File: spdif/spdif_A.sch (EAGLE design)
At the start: 23 parts, among them U1 NC7WZ240, U2 NC7WZ240, U3 FIN1002, U4 NC7SZ175, U5 NC7SZ175

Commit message: spdif: WIP schematic
Signed-off-by: malo <pavol.malosek@gmail.com>
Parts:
- added C10, C11, C12, C13, C9: 100n, 0603, rcl:C-EUC0603
- added D1: PESD0603-240, 25cmsquare:ZDPESD0603-240
- added FB1, FB2: (no value), 25cmsquare:FB_0603
- added JP1, JP2: (no value), 25pinhead:PINHD-2X6/90
- added PWR: (no value), 25cmsquare:LIWE_12_PIN_PWR7X7_COMPAT
- added R11, R20: 22R, 0603, rcl:R-EU_R0603
- added R12, R13, R18: 220R, 0603, rcl:R-EU_R0603
- added R14, R15: 1k5, 0603, rcl:R-EU_R0603
- added R16: 100R, 0603, rcl:R-EU_R0603
- added R17, R19: 75R, 0603, rcl:R-EU_R0603
- added RX0: PLR135/T10, 25cmsquare:PLR135_T10
- added RX1, RX2, TX1, TX2: RCJ-01X, CP-1400-ND, 25cmsquare:RCJ-01X
- added T1, T2: DA101MC, 25cmsquare:DA101MC
- added TP0, TP1, TP10, TP11, TP12, TP13, TP2, TP3, TP4, TP5, TP6, TP7, TP8, TP9: TPB1,27, testpad:TPB1,27
- added TX0: PLT133/T10W, 25cmsquare:PLT133_T10W
- added U6: FIN1002, 25cmsquare:FIN1002
- R3: value 22R, 0603 -> 75R, 0603
- U1: value NC7WZ240 -> NC7SZ175; device 25cmsquare:NC7WZ240 -> 25cmsquare:NC7SZ175
- U2: value NC7WZ240 -> FIN1001; device 25cmsquare:NC7WZ240 -> 25cmsquare:FIN1001
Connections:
- removed net CLK: U4.CP, U5.CP
- removed net NSEL_0: U1_A.~OE1
- removed net NSEL_1: U1_B.~OE1
- removed net NSEL_2: U2_A.~OE1
- removed net NSEL_3: U2_B.~OE1
- removed net SPDIF_IN: R3.2
- removed net TX_COAXIAL: U5.D
- removed net TX_OPTICAL: U4.D
- new net +1V0: PWR.2
- new net +2V5: PWR.1
- new net +5V: PWR.6
- new net CLK_0: JP2.3, U4.CP
- new net CLK_1: JP2.7, U5.CP
- new net CLK_2: JP2.11, U1.CP
- new net N$13: C7.1, R13.2
- new net N$16: R15.2, R16.2, T1.4, TP2.TP, U6.RIN-
- new net N$17: R14.1, R16.1, T1.6, TP3.TP, U6.RIN+
- new net N$18: R12.1, R19.2, T2.1
- new net N$19: R3.1, T2.6, TX2.SIG
- new net N$20: R17.2, RX1.GND1, RX1.GND2, RX1.GND3, T1.3
- new net N$21: R17.1, RX1.SIG, T1.1
- new net N$22: R3.2, T2.4, TX2.GND1, TX2.GND2, TX2.GND3
- new net N$23: R18.2, TP12.TP, U2.ROUT-
- new net N$24: R20.1, TP10.TP, U2.RIN
- new net SPDIF0_IN: R1.1, RX0.OUT
- new net SPDIF_IN_0: JP1.1, JP1.3, R1.2, TP1.TP
- new net SPDIF_IN_1: JP1.5, JP1.7, R11.2, TP4.TP
- new net SPDIF_IN_2: JP1.11, JP1.9, R2.2, TP8.TP
- new net SPDIF_OUT_0: JP2.1, U4.D
- new net SPDIF_OUT_1: JP2.5, U5.D
- new net SPDIF_OUT_2: JP2.9, U1.D
- net +3V3: now also C1.2, C10.2, C12.2, C13.2, C2.2, FB1.P$2, FB2.P$2, PWR.4, R14.2, U1.VCC, U1.~C, U2.VCC, U6.VCC; no longer C1.1, C2.1, U1_PWR.VCC, U2_PWR.VCC
- net GND: now also C1.1, C10.1, C11.1, C12.1, C13.1, C2.1, C9.1, D1.A, JP1.10, JP1.12, JP1.2, JP1.4, JP1.6, JP1.8, JP2.10, JP2.12, JP2.2, JP2.4, JP2.6, JP2.8, PWR.3, PWR.8, R15.1, RX0.GND, RX2.GND1, RX2.GND2, RX2.GND3, TX0.GND, TX1.GND1, TX1.GND2, TX1.GND3, U1.GND, U2.GND, U6.GND; no longer C1.2, C2.2, U1_PWR.GND, U2_PWR.GND
- net N$1: now also R20.2, U1.Q; no longer R1.2, U1_A.A1
- net N$10: now also R12.2, TP11.TP, U2.ROUT+; no longer R2.2, U2_B.A1
- net N$11: now also TP7.TP
- net N$12: now also TP6.TP
- net N$14: now also TP9.TP, TX0.IN
- net N$2: now also R18.1, R19.1, T2.3; no longer U1_B.A1
- net N$4: now also TP5.TP
- net N$5: now also C9.2, FB1.P$1, RX0.VCC; no longer R3.1, U1_A.Y1, U1_B.Y1, U2_A.Y1, U2_B.Y1
- net N$6: now also D1.C, RX2.SIG
- net N$7: now also R11.1, U6.ROUT; no longer R1.1
- net N$8: now also R13.1, TP13.TP, TX1.SIG; no longer C7.1
- net N$9: now also C11.2, FB2.P$1, TX0.VCC; no longer U2_A.A1
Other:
- note added: "16.11.22.A"
- moved on the sheet: C3, C4, C5, C6, C7, C8, R1, R10, R2, R4, R5, R6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

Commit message: spdif: WIP pcb
Signed-off-by: malo <pavol.malosek@gmail.com>
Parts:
- removed TP0: TPB1,27, testpad:TPB1,27
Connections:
- net N$1 renamed Q
- net N$10 renamed FIN_OUT_P
- net N$14 renamed TX0_IN
- net N$18 renamed DA_P
- net N$19 renamed TX2_P
- net N$2 renamed DA_N
- net N$22 renamed TX2_N
- net N$23 renamed FIN_OUT_N
- net N$24 renamed FIN_IN
- net N$9 renamed TX0_VCC
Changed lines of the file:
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@@
 <grid distance="0.1" unitdist="inch" unit="inch" style="lines" multiple="1" display="no" altdistance="0.01" altunitdist="inch" altunit="inch"/>
 <layers>
-<layer number="1" name="Top" color="4" fill="1" visible="yes" active="no"/>
-<layer number="16" name="Bottom" color="1" fill="1" visible="yes" active="no"/>
-<layer number="17" name="Pads" color="2" fill="1" visible="yes" active="no"/>
-<layer number="18" name="Vias" color="2" fill="1" visible="yes" active="no"/>
-<layer number="19" name="Unrouted" color="6" fill="1" visible="yes" active="no"/>
-<layer number="20" name="Dimension" color="15" fill="1" visible="yes" active="no"/>
-<layer number="21" name="tPlace" color="7" fill="1" visible="yes" active="no"/>
-<layer number="22" name="bPlace" color="7" fill="1" visible="yes" active="no"/>
-<layer number="23" name="tOrigins" color="15" fill="1" visible="yes" active="no"/>
-<layer number="24" name="bOrigins" color="15" fill="1" visible="yes" active="no"/>
-<layer number="25" name="tNames" color="7" fill="1" visible="yes" active="no"/>
-<layer number="26" name="bNames" color="7" fill="1" visible="yes" active="no"/>
-<layer number="27" name="tValues" color="7" fill="1" visible="yes" active="no"/>
-<layer number="28" name="bValues" color="7" fill="1" visible="yes" active="no"/>
+<layer number="1" name="Top" color="4" fill="1" visible="no" active="no"/>
+<layer number="16" name="Bottom" color="1" fill="1" visible="no" active="no"/>
+<layer number="17" name="Pads" color="2" fill="1" visible="no" active="no"/>
+<layer number="18" name="Vias" color="2" fill="1" visible="no" active="no"/>
+<layer number="19" name="Unrouted" color="6" fill="1" visible="no" active="no"/>
+<layer number="20" name="Dimension" color="15" fill="1" visible="no" active="no"/>
+<layer number="21" name="tPlace" color="7" fill="1" visible="no" active="no"/>
+<layer number="22" name="bPlace" color="7" fill="1" visible="no" active="no"/>
+<layer number="23" name="tOrigins" color="15" fill="1" visible="no" active="no"/>
+<layer number="24" name="bOrigins" color="15" fill="1" visible="no" active="no"/>
+<layer number="25" name="tNames" color="7" fill="1" visible="no" active="no"/>
+<layer number="26" name="bNames" color="7" fill="1" visible="no" active="no"/>
+<layer number="27" name="tValues" color="7" fill="1" visible="no" active="no"/>
+<layer number="28" name="bValues" color="7" fill="1" visible="no" active="no"/>
 <layer number="29" name="tStop" color="7" fill="3" visible="no" active="no"/>
 <layer number="30" name="bStop" color="7" fill="6" visible="no" active="no"/>
@@
 <layer number="35" name="tGlue" color="7" fill="4" visible="no" active="no"/>
 <layer number="36" name="bGlue" color="7" fill="5" visible="no" active="no"/>
-<layer number="37" name="tTest" color="7" fill="1" visible="yes" active="no"/>
-<layer number="38" name="bTest" color="7" fill="1" visible="yes" active="no"/>
+<layer number="37" name="tTest" color="7" fill="1" visible="no" active="no"/>
+<layer number="38" name="bTest" color="7" fill="1" visible="no" active="no"/>
 <layer number="39" name="tKeepout" color="4" fill="11" visible="no" active="no"/>
 <layer number="40" name="bKeepout" color="1" fill="11" visible="no" active="no"/>
@@
 <layer number="44" name="Drills" color="7" fill="1" visible="no" active="no"/>
 <layer number="45" name="Holes" color="7" fill="1" visible="no" active="no"/>
-<layer number="46" name="Milling" color="3" fill="1" visible="yes" active="no"/>
-<layer number="47" name="Measures" color="7" fill="1" visible="yes" active="no"/>
-<layer number="48" name="Document" color="7" fill="1" visible="yes" active="no"/>
-<layer number="49" name="Reference" color="7" fill="1" visible="yes" active="no"/>
-<layer number="50" name="dxf" color="7" fill="1" visible="yes" active="no"/>
-<layer number="51" name="tDocu" color="7" fill="1" visible="yes" active="no"/>
-<layer number="52" name="bDocu" color="7" fill="1" visible="yes" active="no"/>
-<layer number="53" name="tGND_GNDA" color="7" fill="9" visible="yes" active="no"/>
-<layer number="54" name="bGND_GNDA" color="1" fill="9" visible="yes" active="no"/>
-<layer number="56" name="wert" color="7" fill="1" visible="yes" active="no"/>
-<layer number="57" name="tCAD" color="7" fill="1" visible="yes" active="no"/>
-<layer number="59" name="Invisible" color="7" fill="1" visible="yes" active="no"/>
-<layer number="61" name="stand" color="7" fill="1" visible="yes" active="no"/>
+<layer number="46" name="Milling" color="3" fill="1" visible="no" active="no"/>
+<layer number="47" name="Measures" color="7" fill="1" visible="no" active="no"/>
+<layer number="48" name="Document" color="7" fill="1" visible="no" active="no"/>
+<layer number="49" name="Reference" color="7" fill="1" visible="no" active="no"/>
+<layer number="50" name="dxf" color="7" fill="1" visible="no" active="no"/>
+<layer number="51" name="tDocu" color="7" fill="1" visible="no" active="no"/>
+<layer number="52" name="bDocu" color="7" fill="1" visible="no" active="no"/>
+<layer number="53" name="tGND_GNDA" color="7" fill="9" visible="no" active="no"/>
+<layer number="54" name="bGND_GNDA" color="1" fill="9" visible="no" active="no"/>
+<layer number="56" name="wert" color="7" fill="1" visible="no" active="no"/>
+<layer number="57" name="tCAD" color="7" fill="1" visible="no" active="no"/>
+<layer number="59" name="Invisible" color="7" fill="1" visible="no" active="no"/>
+<layer number="61" name="stand" color="7" fill="1" visible="no" active="no"/>
 <layer number="90" name="Modules" color="5" fill="1" visible="yes" active="yes"/>
 <layer number="91" name="Nets" color="2" fill="1" visible="yes" active="yes"/>
@@
 <part name="T1" library="25cmsquare" deviceset="DA" device="101MC"/>
 <part name="T2" library="25cmsquare" deviceset="DA" device="101MC"/>
-<part name="TP0" library="testpad" deviceset="TP" device="B1,27"/>
 <part name="TP1" library="testpad" deviceset="TP" device="B1,27"/>
 <part name="TP2" library="testpad" deviceset="TP" device="B1,27"/>
@@
 <instance part="GND26" gate="1" x="144.78" y="129.54"/>
 <instance part="T1" gate="G$1" x="152.4" y="96.52"/>
-<instance part="TP0" gate="G$1" x="104.14" y="121.92"/>
 <instance part="TP1" gate="G$1" x="83.82" y="96.52" rot="R180"/>
 <instance part="TP2" gate="G$1" x="180.34" y="91.44" rot="R180"/>
@@
 </segment>
 </net>
-<net name="N$14" class="0">
+<net name="TX0_IN" class="0">
 <segment>
 <pinref part="U4" gate="&gt;NAME" pin="Q"/>
@@
 </segment>
 </net>
-<net name="N$9" class="0">
+<net name="TX0_VCC" class="0">
 <segment>
 <pinref part="C11" gate="G$1" pin="2"/>
@@
 </segment>
 </net>
-<net name="N$19" class="0">
+<net name="TX2_P" class="0">
 <segment>
 <pinref part="TX2" gate="G$1" pin="SIG"/>
@@
 </segment>
 </net>
-<net name="N$22" class="0">
+<net name="TX2_N" class="0">
 <segment>
 <pinref part="TX2" gate="G$1" pin="GND1"/>
@@
 </segment>
 </net>
-<net name="N$2" class="0">
+<net name="DA_N" class="0">
 <segment>
 <wire x1="124.46" y1="137.16" x2="121.92" y2="137.16" width="0.1524" layer="91"/>
@@
 </segment>
 </net>
-<net name="N$10" class="0">
+<net name="FIN_OUT_P" class="0">
 <segment>
 <pinref part="U2" gate="G$1" pin="ROUT+"/>
@@
 </segment>
 </net>
-<net name="N$18" class="0">
+<net name="DA_P" class="0">
 <segment>
 <pinref part="R12" gate="G$1" pin="1"/>
@@
 </segment>
 </net>
-<net name="N$23" class="0">
+<net name="FIN_OUT_N" class="0">
 <segment>
 <pinref part="R18" gate="G$1" pin="2"/>
@@
 </segment>
 </net>
-<net name="N$1" class="0">
+<net name="Q" class="0">
 <segment>
 <pinref part="U1" gate="&gt;NAME" pin="Q"/>
@@
 </segment>
 </net>
-<net name="N$24" class="0">
+<net name="FIN_IN" class="0">
 <segment>
 <pinref part="R20" gate="G$1" pin="1"/>

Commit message: spdif: finished PCB
Signed-off-by: malo <pavol.malosek@gmail.com>
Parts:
- removed R16: 100R, 0603, rcl:R-EU_R0603
- removed R19, R3: 75R, 0603, rcl:R-EU_R0603
- added 3V3, GND, GND33: TEST-22-MULTICOMP, 25cmsquare:TEST-22-MULTICOMP
- R12, R18: value 220R, 0603 -> 36R, 0603
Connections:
- net +3V3: now also 3V3.1
- net DA_N: no longer R19.1
- net DA_P: no longer R19.2
- net GND: now also GND.1, GND33.1, RX1.GND1, RX1.GND2, RX1.GND3; no longer RX2.GND1, RX2.GND2, RX2.GND3
- net N$16: no longer R16.2
- net N$17: no longer R16.1
- net N$20: now also RX2.GND2; no longer RX1.GND1, RX1.GND2, RX1.GND3
- net N$21: now also RX2.SIG; no longer RX1.SIG
- net N$6: now also RX1.SIG; no longer RX2.SIG
- net SPDIF_IN_0: now also JP1.11, JP1.9; no longer JP1.1, JP1.3
- net SPDIF_IN_1: now also R2.2, TP8.TP; no longer R11.2, TP4.TP
- net SPDIF_IN_2: now also JP1.1, JP1.3, R11.2, TP4.TP; no longer JP1.11, JP1.9, R2.2, TP8.TP
- net TX2_N: no longer R3.2, TX2.GND2, TX2.GND3
- net TX2_P: no longer R3.1
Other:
- moved on the sheet: R12, R14, R15, R17, R18, RX1, RX2, T1, T2, TP11, TP12, TX2

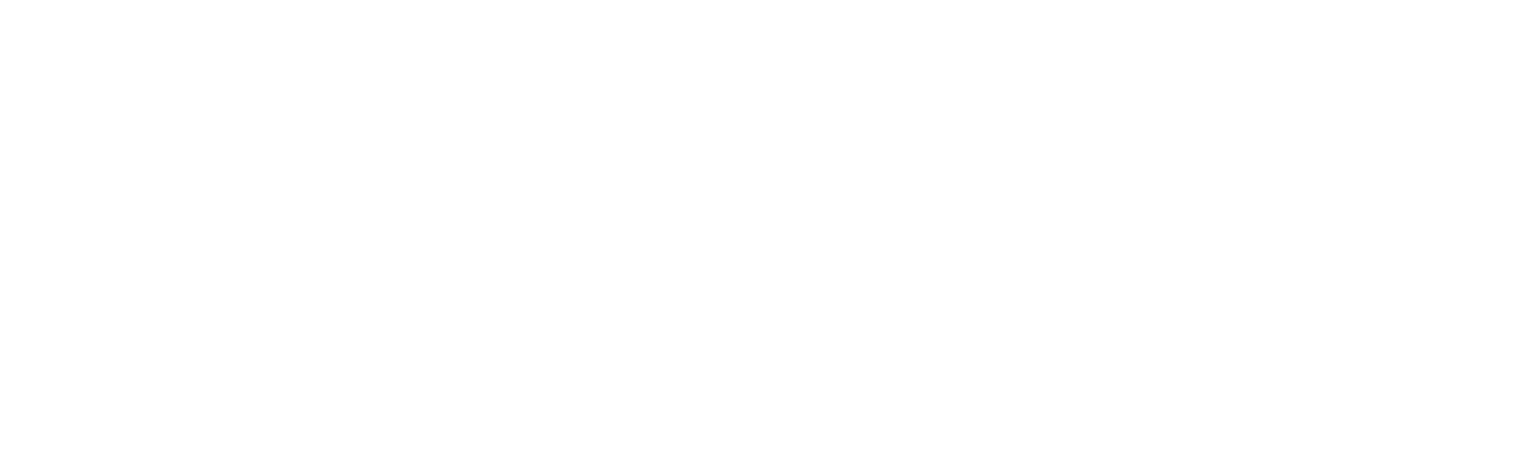
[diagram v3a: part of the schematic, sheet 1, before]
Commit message: spdif: added partlist for digikey
Signed-off-by: malo <pavol.malosek@gmail.com>
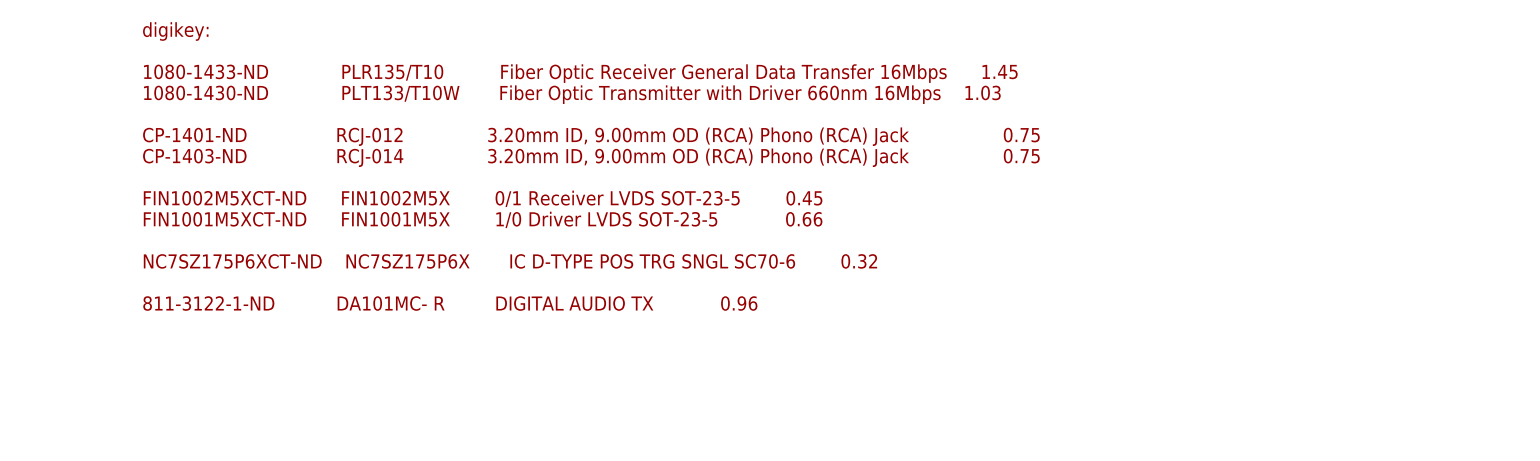
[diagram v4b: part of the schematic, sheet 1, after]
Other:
- note added: "digikey: 1080-1433-ND PLR135/T10 Fiber Optic Receiver General Data Transfer 16Mbps 1.45 1080-1430-ND PLT133/T10W Fiber Optic Transmitter with Driver 660nm 16Mbps 1.03 CP-1401-ND RCJ-012 3.20mm ID, 9.00mm OD (RCA) Phono (RCA) Jack 0.75 CP-1403-ND RCJ-014 3.20mm ID, 9.00mm OD (RCA) Phono (RCA) Jack 0.75 FIN1002M5XCT-ND FIN1002M5X 0/1 Receiver LVDS SOT-23-5 0.45 FIN1001M5XCT-ND FIN1001M5X 1/0 Driver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"
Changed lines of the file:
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@@
 <plain>
 <text x="167.64" y="10.16" size="6.4516" layer="94">16.11.22.A</text>
+<text x="266.7" y="134.62" size="1.778" layer="94">digikey:
+1080-1433-ND             PLR135/T10          Fiber Optic Receiver General Data Transfer 16Mbps  	1.45
+1080-1430-ND             PLT133/T10W       Fiber Optic Transmitter with Driver 660nm 16Mbps	1.03
+CP-1401-ND                RCJ-012               3.20mm ID, 9.00mm OD (RCA) Phono (RCA) Jack                 0.75
+CP-1403-ND                RCJ-014               3.20mm ID, 9.00mm OD (RCA) Phono (RCA) Jack                 0.75
+FIN1002M5XCT-ND      FIN1002M5X        0/1 Receiver LVDS SOT-23-5		0.45
+FIN1001M5XCT-ND      FIN1001M5X        1/0 Driver LVDS SOT-23-5			0.66
+NC7SZ175P6XCT-ND    NC7SZ175P6X       IC D-TYPE POS TRG SNGL SC70-6		0.32
+811-3122-1-ND           DA101MC- R         DIGITAL AUDIO TX			0.96</text>
 </plain>
 <instances>
@@
 </schematic>
 </drawing>
+<compatibility>
+<note version="6.3" minversion="6.2.2" severity="warning">
+Since Version 6.2.2 text objects can contain more than one line,
+which will not be processed correctly with this version.
+</note>
+</compatibility>
 </eagle>
